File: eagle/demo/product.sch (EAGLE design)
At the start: 46 parts, among them IC101 MCU, T101 BC548C, X1 MALE_2X10-T-VERTICAL_2.54MM, X2 MALE_2X1-T-VERTICAL, X3 MALE_2X1-T-VERTICAL, X302 MALE_2X10-T-VERTICAL_2.54MM, X4 CLAMP_1X2-T-2.5MM, X5 MALE_2X1-T-VERTICAL, X6 CLAMP_1X2-T-2.5MM, X7 MALE_2X1-T-VERTICAL, X8 CLAMP_1X2-T-2.5MM

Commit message: step 2: delete dev. pages
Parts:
- removed C301: 10U, be_rcl:C_POL_S_6032
- removed FD1, FD2, FD3, FD301, FD302, FD4, FD5, FD6: FIDUCIAL_CROSSHAIR, be_marks:FIDUCIAL_CROSSHAIR
- removed H1, H2, H3, H301, H302, H303, H304, H4, H5, H6, H7, H8: HOLE_3.2_PAD, be_holes:HOLE_3.2_PAD
- removed LED3, LED4: (no value), be_opt:LED_S_0805
- removed R3, R4: 330, be_rcl:R_S_0805
- removed X1, X302: MALE_2X10-T-VERTICAL_2.54MM, be_con_jump:MALE_2X10-T-VERTICAL_2.54MM
- removed X2, X3, X5, X7: MALE_2X1-T-VERTICAL, be_con_jump:MALE_2X1-T-VERTICAL
- removed X301: (no value), be_con_jump:POWER_JACK-T-0
- removed X6, X8: CLAMP_1X2-T-2.5MM, be_con_jump:CLAMP_1X2-T-2.5MM
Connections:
- removed net SH_DBG_CLK: LED3.A, R3.1
- removed net SH_DBG_DRV: LED4.A, R4.1
- net GND: no longer C301.-, LED3.C, LED4.C, X1.1, X1.3, X2.1, X3.1, X301.1, X302.1, X302.3, X5.1, X6.1, X7.1, X8.1
- net KBD_OUT: no longer R3.2, X3.2, X7.2
- net LED_DRV_IN: no longer R4.2, X2.2, X5.2
- net MCU_CLK: no longer X1.2, X302.2
- net MCU_QD: no longer X1.4, X302.4
- net P5V: no longer C301.+, X301.3, X6.2, X8.2

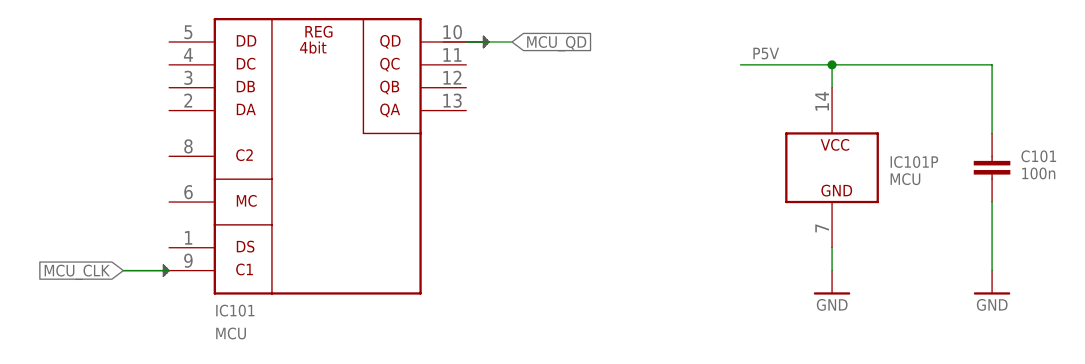
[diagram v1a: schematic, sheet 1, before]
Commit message: step 3a: reduce routing page
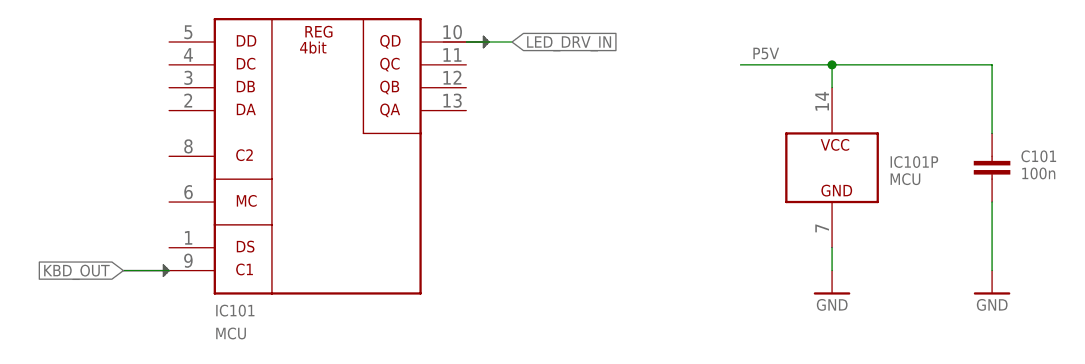
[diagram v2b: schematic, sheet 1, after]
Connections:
- removed net MCU_CLK: IC101G$1.C1, N2.2
- removed net MCU_QD: IC101G$1.QD, N1.2
- net KBD_OUT: now also IC101G$1.C1, N2.2
- net LED_DRV_IN: now also IC101G$1.QD, N1.2
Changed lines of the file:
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@@
 </segment>
 </net>
-<net name="MCU_CLK" class="0">
+<net name="KBD_OUT" class="0">
 <segment>
 <pinref part="IC101" gate="G$1" pin="C1"/>
@@
 </segment>
 </net>
-<net name="MCU_QD" class="0">
+<net name="LED_DRV_IN" class="0">
 <segment>
 <pinref part="IC101" gate="G$1" pin="QD"/>
@@
 </busses>
 <nets>
-<net name="MCU_QD" class="0">
-<segment>
-<pinref part="N1" gate="G$1" pin="2"/>
-<wire x1="157.48" y1="53.34" x2="149.86" y2="53.34" width="0.1524" layer="91"/>
-<label x="149.86" y="53.34" size="1.27" layer="95" font="fixed" rot="R180" xref="yes"/>
-</segment>
-</net>
 <net name="LED_DRV_IN" class="0">
 <segment>
@@
 <label x="180.34" y="53.34" size="1.27" layer="95" font="fixed" xref="yes"/>
 </segment>
-</net>
-<net name="MCU_CLK" class="0">
 <segment>
-<pinref part="N2" gate="G$1" pin="2"/>
-<wire x1="157.48" y1="45.72" x2="149.86" y2="45.72" width="0.1524" layer="91"/>
-<label x="149.86" y="45.72" size="1.27" layer="95" font="fixed" rot="R180" xref="yes"/>
+<pinref part="N1" gate="G$1" pin="2"/>
+<wire x1="157.48" y1="53.34" x2="149.86" y2="53.34" width="0.1524" layer="91"/>
+<label x="149.86" y="53.34" size="1.27" layer="95" font="fixed" rot="R180" xref="yes"/>
 </segment>
 </net>
@@
 <label x="180.34" y="45.72" size="1.27" layer="95" font="fixed" xref="yes"/>
 </segment>
+<segment>
+<pinref part="N2" gate="G$1" pin="2"/>
+<wire x1="157.48" y1="45.72" x2="149.86" y2="45.72" width="0.1524" layer="91"/>
+<label x="149.86" y="45.72" size="1.27" layer="95" font="fixed" rot="R180" xref="yes"/>
+</segment>
 </net>

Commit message: step 3b: remove routing page
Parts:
- removed N1: NET_CHANGER-S-0.3MM, be_con_jump:NET_CHANGER-S-0.3MM
- removed N2: NET_CHANGER-S-0.15MM, be_con_jump:NET_CHANGER-S-0.15MM
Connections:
- net KBD_OUT: no longer N2.1, N2.2
- net LED_DRV_IN: no longer N1.1, N1.2
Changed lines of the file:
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@@
 <part name="U$3" library="be_info" deviceset="ARROW_1" device=""/>
 <part name="U$4" library="be_info" deviceset="ARROW_1" device=""/>
-<part name="FRAME_NET_CHANGERS1" library="be_frame" deviceset="A4_LANDSCAPE_NET_CHANGERS" device=""/>
-<part name="N1" library="be_con_jump" deviceset="NET_CHANGER" device="-S-0.3MM"/>
-<part name="U$6" library="be_info" deviceset="ARROW_1" device=""/>
-<part name="U$7" library="be_info" deviceset="ARROW_1" device=""/>
-<part name="N2" library="be_con_jump" deviceset="NET_CHANGER" device="-S-0.15MM" value="NET_CHANGER-S-0.15MM"/>
-<part name="U$8" library="be_info" deviceset="ARROW_1" device=""/>
-<part name="U$9" library="be_info" deviceset="ARROW_1" device=""/>
 <part name="FRAME_PRODUCT2" library="be_frame" deviceset="A4_LANDSCAPE_PRODUCT" device="">
 <attribute name="DESCRIPTION" value="LED driver"/>
@@
 </segment>
 </net>
-</nets>
-</sheet>
-<sheet>
-<description>routing</description>
-<plain>
-</plain>
-<instances>
-<instance part="FRAME_NET_CHANGERS1" gate="G$1" x="0" y="0"/>
-<instance part="N1" gate="G$1" x="165.1" y="53.34" rot="MR0"/>
-<instance part="U$6" gate="G$1" x="175.26" y="53.34" rot="R180"/>
-<instance part="U$7" gate="G$1" x="152.4" y="53.34" rot="R180"/>
-<instance part="N2" gate="G$1" x="165.1" y="45.72" rot="MR0"/>
-<instance part="U$8" gate="G$1" x="177.8" y="45.72"/>
-<instance part="U$9" gate="G$1" x="154.94" y="45.72"/>
-</instances>
-<busses>
-</busses>
-<nets>
-<net name="LED_DRV_IN" class="0">
-<segment>
-<pinref part="N1" gate="G$1" pin="1"/>
-<wire x1="172.72" y1="53.34" x2="180.34" y2="53.34" width="0.1524" layer="91"/>
-<label x="180.34" y="53.34" size="1.27" layer="95" font="fixed" xref="yes"/>
-</segment>
-<segment>
-<pinref part="N1" gate="G$1" pin="2"/>
-<wire x1="157.48" y1="53.34" x2="149.86" y2="53.34" width="0.1524" layer="91"/>
-<label x="149.86" y="53.34" size="1.27" layer="95" font="fixed" rot="R180" xref="yes"/>
-</segment>
-</net>
-<net name="KBD_OUT" class="0">
-<segment>
-<pinref part="N2" gate="G$1" pin="1"/>
-<wire x1="172.72" y1="45.72" x2="180.34" y2="45.72" width="0.1524" layer="91"/>
-<label x="180.34" y="45.72" size="1.27" layer="95" font="fixed" xref="yes"/>
-</segment>
-<segment>
-<pinref part="N2" gate="G$1" pin="2"/>
-<wire x1="157.48" y1="45.72" x2="149.86" y2="45.72" width="0.1524" layer="91"/>
-<label x="149.86" y="45.72" size="1.27" layer="95" font="fixed" rot="R180" xref="yes"/>
-</segment>
-</net>

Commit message: step 4: add prod. spec. sheet
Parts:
- added X401: (no value), be_con_jump:POWER_JACK-T-0
- renumbered C1 to C201, C2 to C301, R1 to R301, R101 to R201, R102 to R202, S1 to S301, T101 to T201, X4 to X201
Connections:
- net GND: now also X401.2
- net P5V: now also X401.3
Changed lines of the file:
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@@
 <attribute name="DESCRIPTION" value="LED driver"/>
 </part>
-<part name="R101" library="be_rcl" deviceset="R" device="_S_0805" value="2k2"/>
-<part name="T101" library="be_transistor" deviceset="NPN" device="_S_SOT23" value="BC548C"/>
-<part name="R102" library="be_rcl" deviceset="R" device="_S_0805" value="100"/>
+<part name="R201" library="be_rcl" deviceset="R" device="_S_0805" value="2k2"/>
+<part name="T201" library="be_transistor" deviceset="NPN" device="_S_SOT23" value="BC548C"/>
+<part name="R202" library="be_rcl" deviceset="R" device="_S_0805" value="100"/>
 <part name="GND11" library="be_supply" deviceset="GND" device=""/>
-<part name="C1" library="be_rcl" deviceset="C_POL" device="_S_6032" value="100n"/>
+<part name="C201" library="be_rcl" deviceset="C_POL" device="_S_6032" value="100n"/>
 <part name="GND12" library="be_supply" deviceset="GND" device=""/>
-<part name="X4" library="be_con_jump" deviceset="CLAMP_1X2" device="-T-2.5MM">
+<part name="X201" library="be_con_jump" deviceset="CLAMP_1X2" device="-T-2.5MM">
 <attribute name="FUNCTION" value="LED DRV OUT"/>
 </part>
@@
 <attribute name="DESCRIPTION" value="LED driver"/>
 </part>
-<part name="S1" library="be_switch" deviceset="PUSH_BUTTON" device="_S_6X6MM"/>
-<part name="C2" library="be_rcl" deviceset="C" device="_S_0805" value="100n"/>
-<part name="R1" library="be_rcl" deviceset="R" device="_S_0805" value="4k7"/>
+<part name="S301" library="be_switch" deviceset="PUSH_BUTTON" device="_S_6X6MM"/>
+<part name="C301" library="be_rcl" deviceset="C" device="_S_0805" value="100n"/>
+<part name="R301" library="be_rcl" deviceset="R" device="_S_0805" value="4k7"/>
 <part name="GND16" library="be_supply" deviceset="GND" device=""/>
+<part name="FRAME_PRODUCT4" library="be_frame" deviceset="A4_LANDSCAPE_PRODUCT" device=""/>
+<part name="X401" library="be_con_jump" deviceset="POWER_JACK" device="-T-0"/>
+<part name="GND3" library="be_supply" deviceset="GND" device=""/>
 </parts>
 <sheets>
@@
 <instances>
 <instance part="FRAME_PRODUCT2" gate="G$1" x="0" y="0"/>
-<instance part="R101" gate="G$1" x="149.86" y="60.96"/>
-<instance part="T101" gate="G$1" x="160.02" y="60.96"/>
-<instance part="R102" gate="G$1" x="162.56" y="73.66" rot="R90"/>
+<instance part="R201" gate="G$1" x="149.86" y="60.96"/>
+<instance part="T201" gate="G$1" x="160.02" y="60.96"/>
+<instance part="R202" gate="G$1" x="162.56" y="73.66" rot="R90"/>
 <instance part="GND11" gate="1" x="162.56" y="50.8"/>
-<instance part="C1" gate="G$1" x="203.2" y="60.96"/>
+<instance part="C201" gate="G$1" x="203.2" y="60.96"/>
 <instance part="GND12" gate="1" x="203.2" y="50.8"/>
-<instance part="X4" gate="G$1" x="210.82" y="106.68" rot="MR180">
+<instance part="X201" gate="G$1" x="210.82" y="106.68" rot="MR180">
 <attribute name="FUNCTION" x="203.2" y="114.3" size="2.54" layer="96" font="fixed" rot="MR180"/>
 </instance>
@@
 <wire x1="215.9" y1="66.04" x2="203.2" y2="66.04" width="0.1524" layer="91"/>
 <label x="207.01" y="66.675" size="1.27" layer="95" font="fixed"/>
-<pinref part="C1" gate="G$1" pin="+"/>
+<pinref part="C201" gate="G$1" pin="+"/>
 <wire x1="203.2" y1="66.04" x2="198.12" y2="66.04" width="0.1524" layer="91"/>
 <wire x1="203.2" y1="63.5" x2="203.2" y2="66.04" width="0.1524" layer="91"/>
@@
 </segment>
 <segment>
-<pinref part="X4" gate="G$1" pin="1"/>
+<pinref part="X201" gate="G$1" pin="1"/>
 <wire x1="208.28" y1="104.14" x2="195.58" y2="104.14" width="0.1524" layer="91"/>
 <label x="196.215" y="104.775" size="1.27" layer="95" font="fixed"/>
@@
 <net name="GND" class="0">
 <segment>
-<pinref part="T101" gate="G$1" pin="E"/>
+<pinref part="T201" gate="G$1" pin="E"/>
 <wire x1="162.56" y1="55.88" x2="162.56" y2="53.34" width="0.1524" layer="91"/>
 <pinref part="GND11" gate="1" pin="GND"/>
 </segment>
 <segment>
-<pinref part="C1" gate="G$1" pin="-"/>
+<pinref part="C201" gate="G$1" pin="-"/>
 <pinref part="GND12" gate="1" pin="GND"/>
 <wire x1="203.2" y1="55.88" x2="203.2" y2="53.34" width="0.1524" layer="91"/>
@@
 <net name="LED_DRV_IN" class="0">
 <segment>
-<pinref part="R101" gate="G$1" pin="1"/>
+<pinref part="R201" gate="G$1" pin="1"/>
 <wire x1="144.78" y1="60.96" x2="139.7" y2="60.96" width="0.1524" layer="91"/>
 <label x="139.7" y="60.96" size="1.27" layer="95" font="fixed" rot="R180" xref="yes"/>
@@
 <net name="LED_DRV_B" class="0">
 <segment>
-<pinref part="R101" gate="G$1" pin="2"/>
-<pinref part="T101" gate="G$1" pin="B"/>
+<pinref part="R201" gate="G$1" pin="2"/>
+<pinref part="T201" gate="G$1" pin="B"/>
 <wire x1="154.94" y1="60.96" x2="157.48" y2="60.96" width="0.1524" layer="91"/>
 </segment>
@@
 <net name="LED_DRV_C" class="0">
 <segment>
-<pinref part="T101" gate="G$1" pin="C"/>
-<pinref part="R102" gate="G$1" pin="1"/>
+<pinref part="T201" gate="G$1" pin="C"/>
+<pinref part="R202" gate="G$1" pin="1"/>
 <wire x1="162.56" y1="66.04" x2="162.56" y2="68.58" width="0.1524" layer="91"/>
 </segment>
@@
 <net name="LED_DRV_OUT" class="0">
 <segment>
-<pinref part="R102" gate="G$1" pin="2"/>
+<pinref part="R202" gate="G$1" pin="2"/>
 <wire x1="162.56" y1="78.74" x2="162.56" y2="81.28" width="0.1524" layer="91"/>
 <wire x1="162.56" y1="81.28" x2="172.72" y2="81.28" width="0.1524" layer="91"/>
@@
 </segment>
 <segment>
-<pinref part="X4" gate="G$1" pin="2"/>
+<pinref part="X201" gate="G$1" pin="2"/>
 <wire x1="208.28" y1="106.68" x2="195.58" y2="106.68" width="0.1524" layer="91"/>
 <label x="195.58" y="106.68" size="1.27" layer="95" font="fixed" rot="R180" xref="yes"/>
@@
 <instances>
 <instance part="FRAME_PRODUCT3" gate="G$1" x="0" y="0"/>
-<instance part="S1" gate="G$1" x="175.26" y="66.04"/>
-<instance part="C2" gate="G$1" x="187.96" y="55.88"/>
-<instance part="R1" gate="G$1" x="187.96" y="76.2" rot="R270"/>
+<instance part="S301" gate="G$1" x="175.26" y="66.04"/>
+<instance part="C301" gate="G$1" x="187.96" y="55.88"/>
+<instance part="R301" gate="G$1" x="187.96" y="76.2" rot="R270"/>
 <instance part="GND16" gate="1" x="187.96" y="45.72"/>
 </instances>
@@
 <net name="KBD_RC" class="0">
 <segment>
-<pinref part="R1" gate="G$1" pin="2"/>
-<pinref part="C2" gate="G$1" pin="1"/>
+<pinref part="R301" gate="G$1" pin="2"/>
+<pinref part="C301" gate="G$1" pin="1"/>
 <wire x1="187.96" y1="71.12" x2="187.96" y2="66.04" width="0.1524" layer="91"/>
-<pinref part="S1" gate="G$1" pin="B1"/>
+<pinref part="S301" gate="G$1" pin="B1"/>
 <wire x1="187.96" y1="66.04" x2="187.96" y2="58.42" width="0.1524" layer="91"/>
 <wire x1="180.34" y1="66.04" x2="187.96" y2="66.04" width="0.1524" layer="91"/>
@@
 <net name="P5V" class="0">
 <segment>
-<pinref part="R1" gate="G$1" pin="1"/>
+<pinref part="R301" gate="G$1" pin="1"/>
 <wire x1="187.96" y1="81.28" x2="187.96" y2="86.36" width="0.1524" layer="91"/>
 <wire x1="187.96" y1="86.36" x2="170.18" y2="86.36" width="0.1524" layer="91"/>
@@
 <net name="KBD_OUT" class="0">
 <segment>
-<pinref part="S1" gate="G$1" pin="A1"/>
+<pinref part="S301" gate="G$1" pin="A1"/>
 <wire x1="170.18" y1="66.04" x2="162.56" y2="66.04" width="0.1524" layer="91"/>
 <label x="162.56" y="66.04" size="1.27" layer="95" font="fixed" rot="R180" xref="yes"/>
@@
 <net name="GND" class="0">
 <segment>
-<pinref part="C2" gate="G$1" pin="2"/>
+<pinref part="C301" gate="G$1" pin="2"/>
 <pinref part="GND16" gate="1" pin="GND"/>
 <wire x1="187.96" y1="48.26" x2="187.96" y2="50.8" width="0.1524" layer="91"/>
 </segment>
 </net>
+</nets>
+</sheet>
+<sheet>
+<description>PWR supply</description>
+<plain>
+</plain>
+<instances>
+<instance part="FRAME_PRODUCT4" gate="G$1" x="0" y="0"/>
+<instance part="X401" gate="G$1" x="160.02" y="71.12"/>
+<instance part="GND3" gate="1" x="170.18" y="63.5"/>
+</instances>
+<busses>
+</busses>
+<nets>
+<net name="P5V" class="0">
+<segment>
+<pinref part="X401" gate="G$1" pin="3"/>
+<wire x1="165.1" y1="73.66" x2="177.8" y2="73.66" width="0.1524" layer="91"/>
+<label x="173.355" y="74.295" size="1.27" layer="95" font="fixed"/>
+</segment>
+</net>
+<net name="GND" class="0">
+<segment>
+<pinref part="X401" gate="G$1" pin="2"/>
+<pinref part="GND3" gate="1" pin="GND"/>
+<wire x1="165.1" y1="71.12" x2="170.18" y2="71.12" width="0.1524" layer="91"/>
+<wire x1="170.18" y1="71.12" x2="170.18" y2="66.04" width="0.1524" layer="91"/>
+</segment>
+</net>
